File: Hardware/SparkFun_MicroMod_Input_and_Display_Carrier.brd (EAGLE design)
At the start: 57.1 x 82.5 mm, 72 parts, among them J1 MICROMOD-2222-C, J2 MICRO-SD, J3 USB-C_Prog, J4 AVR_SPI_PROG_3X2TESTPOINTS, J5 2.4" TFT, J6 QWIIC_RIGHT_ANGLE, Q1 1.1A/60V/600mΩ, U2 ATTINY84, U5 AP7361C-33FGE

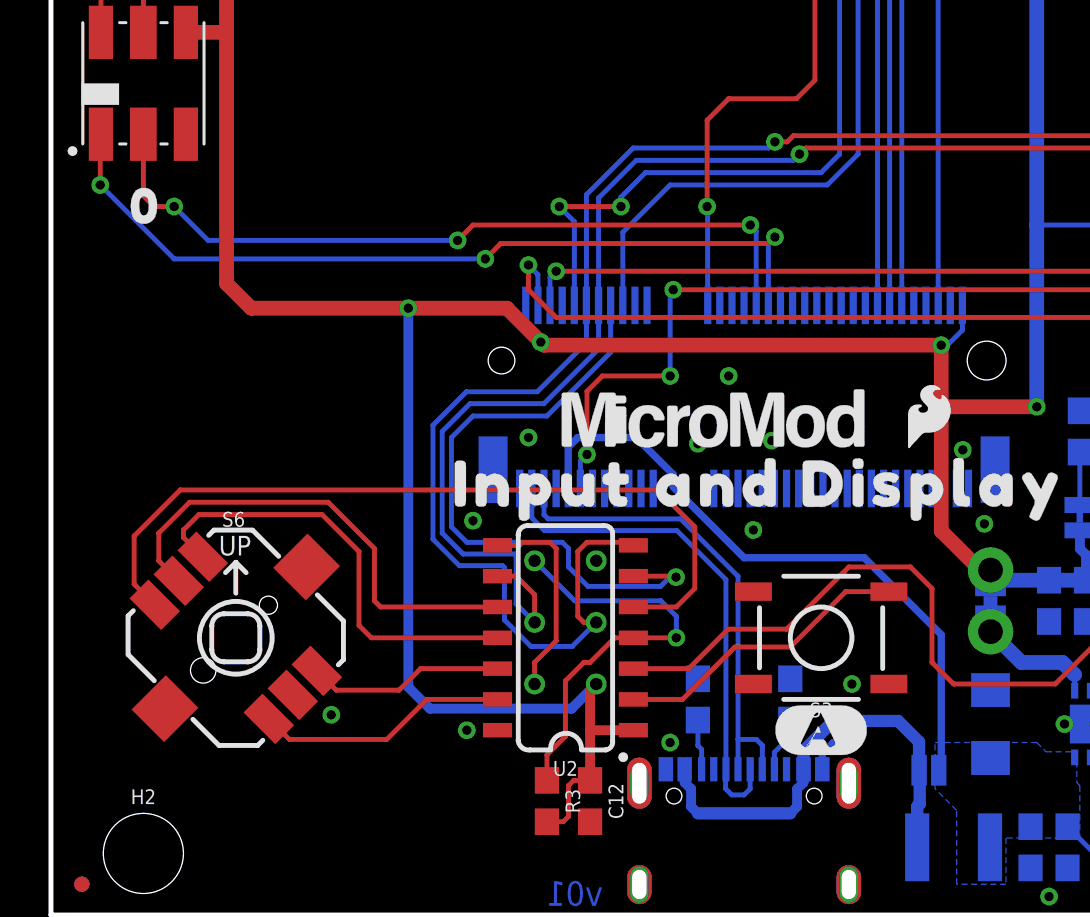
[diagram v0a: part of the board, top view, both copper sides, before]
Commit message: Pre-review changes
Added SWD connector
Updated SPI names
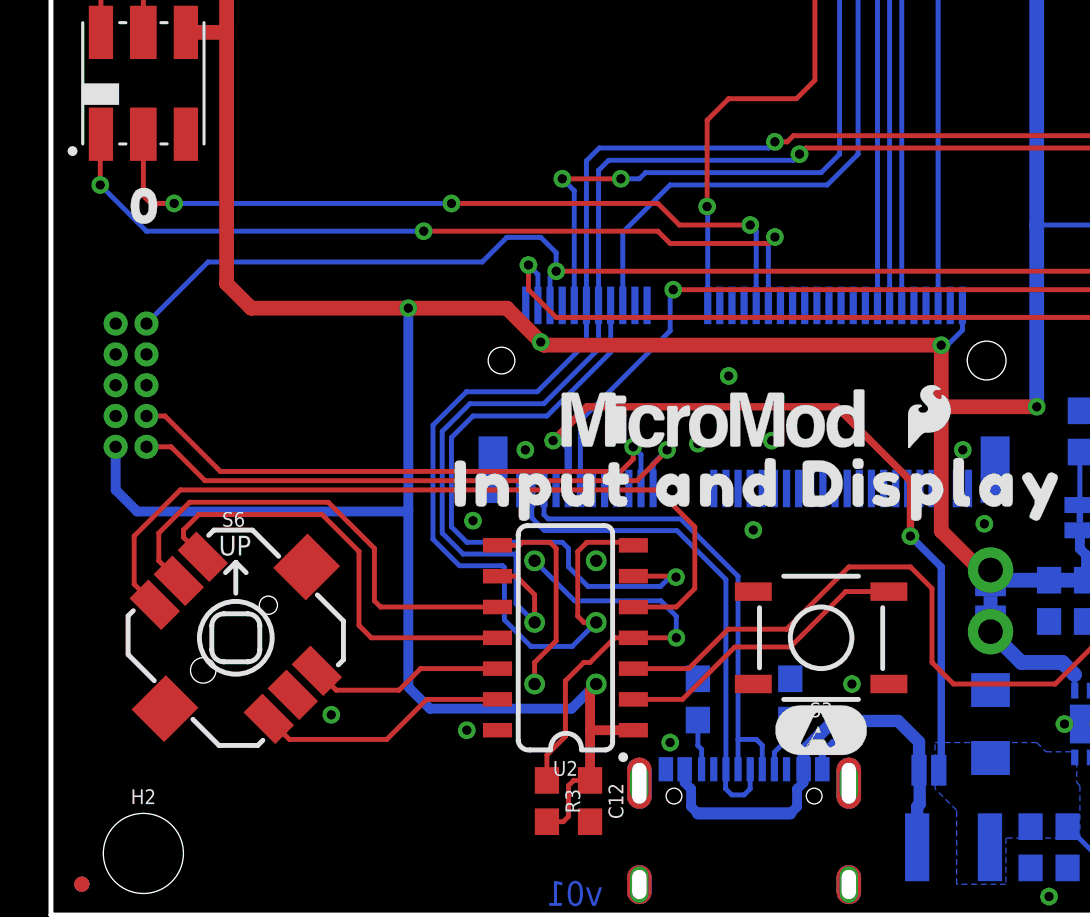
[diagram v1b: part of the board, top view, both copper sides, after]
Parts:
- added J7: CORTEX_JTAG_DEBUG, SparkFun-Connectors:2X5-PTH-1.27MM-NO_SILK
- added U$14: (no value), output:#BYP#0
- added U$15: (no value), output:#SWD#0
- H5: value STAND-OFF-REFLOW2.5MM_TALL -> STAND-OFF
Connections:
- net SPI_MISO renamed SPI_CIPO
- net SPI_MOSI renamed SPI_COPI
- removed net N$17: J1.23
- removed net N$18: J1.21
- new net SWDCK: J1.21, J7.4
- new net SWDIO: J1.23, J7.2
- net !RESET: now also J7.10
- net 3.3V: now also J7.1
- net GND: now also J7.3, J7.5, J7.9
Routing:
- net SWDIO: track 0.00 -> 24.4 mm, vias 0 -> 1
- net SWDCK: track 0.00 -> 23.6 mm, vias 0 -> 1
- net !RESET: track 38.1 -> 57.5 mm
- net 3.3V: track 251.4 -> 265.6 mm
- net VIN: track 29.0 -> 34.0 mm, vias 0 -> 2
- net !BOOT: track 50.5 -> 48.9 mm, vias 4 -> 2
- net SDA: track 71.0 -> 71.8 mm
- net SCL: track 62.2 -> 62.8 mm
- net LED_DATA: track 34.5 -> 34.0 mm
- net LED_CLK: track 32.0 -> 31.5 mm

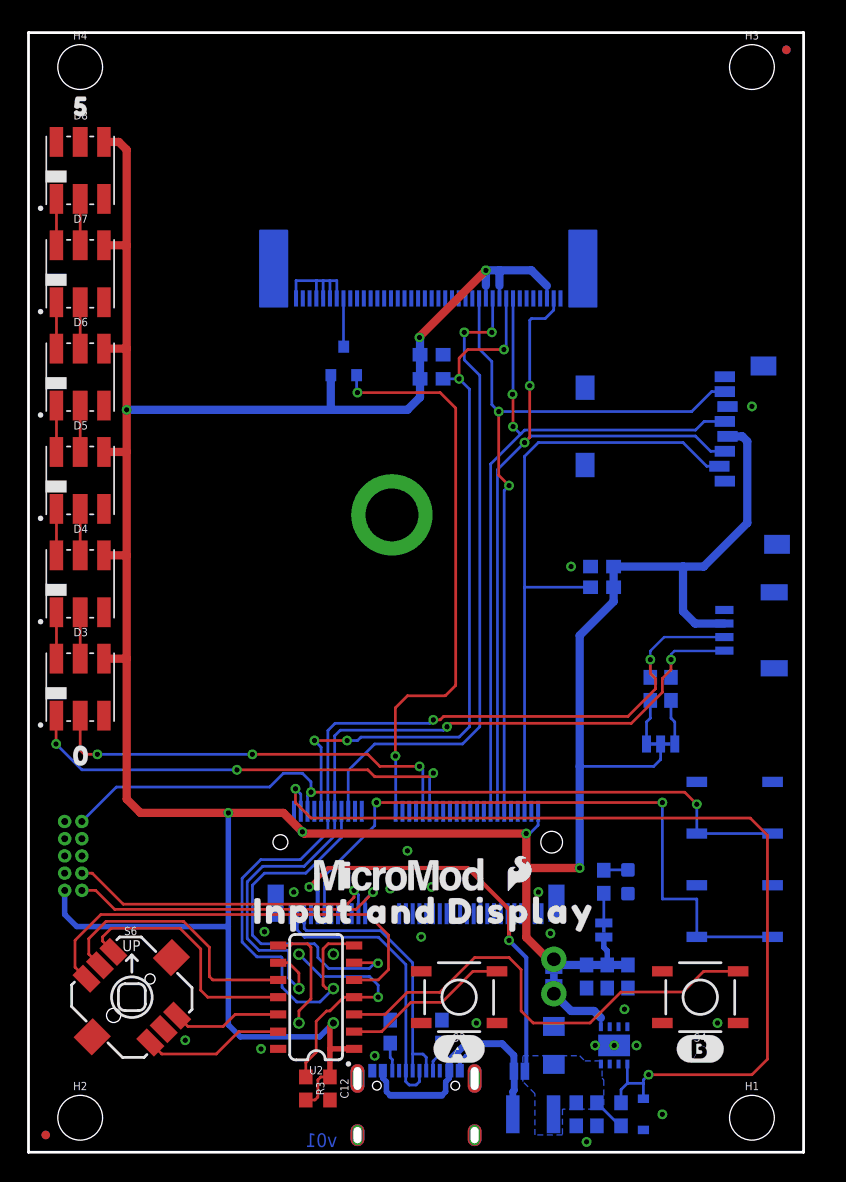
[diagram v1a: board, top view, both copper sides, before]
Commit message: Post review changes
- Added notes for jumpers
- Changed SPI_CS to SD_CS label
- Connected display reset to IO
- Added NO jumper between MicroMod and regulator enable
- Added Buzzer to PWM1
- Broke out A0/1, RX1/TX1, CAN-RX/TX, 3.3V, and GND
- Added name on back of the board
- Fixed or corrected DRC errors
- Fixed non-mitered corners
- Moved reset and boot buttons
- Added indicator for "UP" on 5-way switch
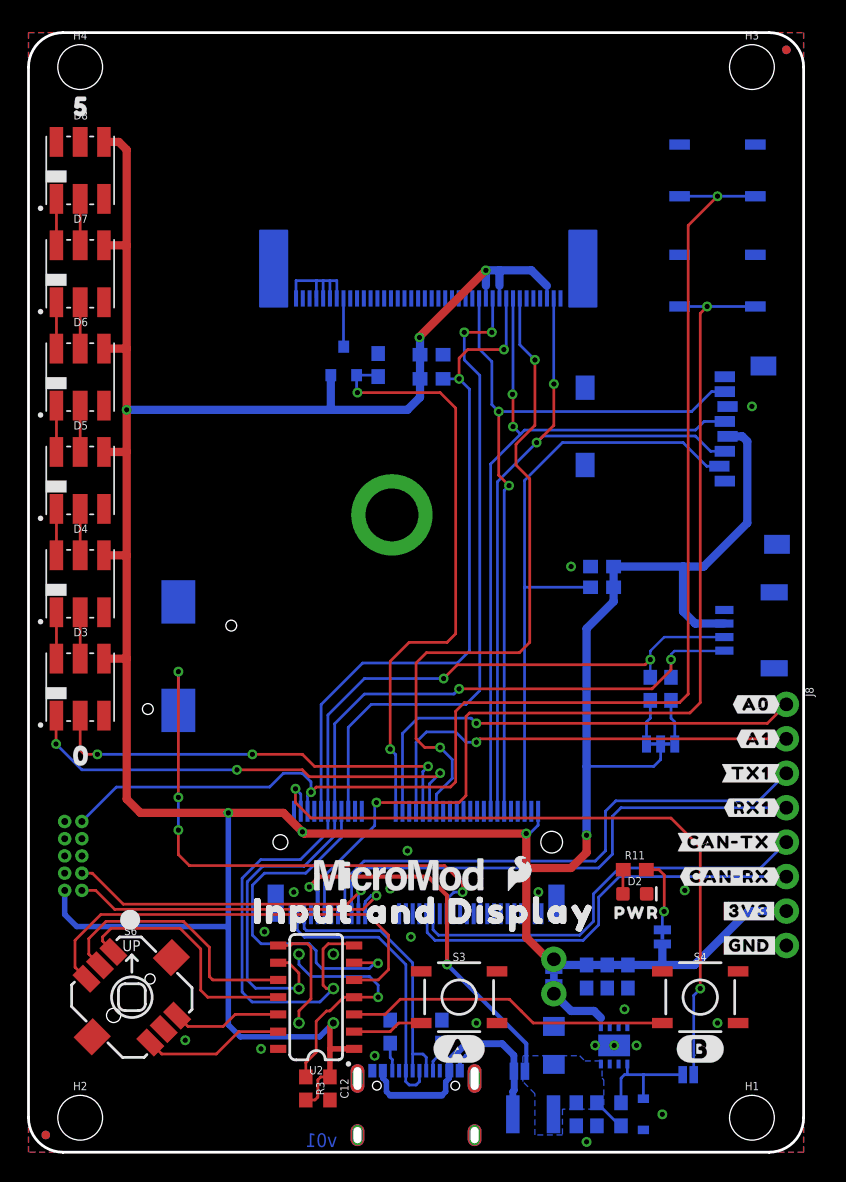
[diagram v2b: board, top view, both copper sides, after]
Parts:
- added 3V3_EN: (no value), SparkFun-Jumpers:SMT-JUMPER_2_NO_SILK
- added J8: (no value), SparkFun-Connectors:1X08_NO_SILK
- added LS1: Buzzer, SparkFun-Electromechanical:BUZZER-CCV
- added R9: 10k, SparkFun-Resistors:0603
- added U$16, U$17: (no value), output:INPUT_AND_DISPLAY0
- added U$19: (no value), output:#PWR#0
- added U$20: (no value), output:#3V3_CTRL#0
- added U$21: (no value), output:#PWM1#0
- added U$22, U$23: (no value), output:#A0#0
- added U$24, U$25: (no value), output:#A1#0
- added U$26, U$27: (no value), output:#TX1#0
- added U$28, U$31: (no value), output:#3V3#0
- added U$29, U$30: (no value), output:#GND#0
- added U$32, U$33: (no value), output:#RX1#0
- added U$34, U$35: (no value), output:#CAN#RX#0
- added U$36, U$37: (no value), output:#CAN#TX#0
- J6: value QWIIC_RIGHT_ANGLE -> QWIIC_RA
- moved S1 47.0 mm to (50.8, 72.4)
- moved U$4 46.6 mm to (50.8, 60.6)
- moved S2 46.5 mm to (50.8, 64.3)
- moved U$9 39.4 mm to (50.8, 69.0)
- moved PWR 4.35 mm to (46.7, 15.9)
- moved R11 2.45 mm to (44.7, 20.8), flipped to the top, turned to 0 degrees
- moved LOGO1 1.53 mm to (11.4, 54.4)
- moved U$13 1.31 mm to (44.8, 17.7), flipped to the top, turned to 0 degrees
- moved D2 1.02 mm to (44.7, 19.1), flipped to the top, turned to 0 degrees
- turned S3 to 0 degrees
- turned S4 to 0 degrees
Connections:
- net SPI_!CS renamed SD_!CS
- removed net DISP_TE: J1.47
- new net A0: J1.34, J8.1
- new net A1: J1.38, J8.2
- new net BUZZER: J1.47, LS1.-
- new net CAN-RX: J1.41, J8.6
- new net CAN-TX: J1.43, J8.5
- new net ENABLE: 3V3_EN.2, D1.C, R5.1, U5.5
- new net RX1: J1.19, J8.4
- new net TX1: J1.17, J8.3
- net 3.3V: now also J8.7
- net 3.3V_EN: now also 3V3_EN.1; no longer D1.C, R5.1, U5.5
- net DISP_!RST: now also J1.44
- net DISP_BL: now also R9.2
- net GND: now also J8.8, LS1.+, R9.1
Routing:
- net DISP_!RST: track 0.00 -> 49.0 mm, vias 0 -> 2
- net BUZZER: track 0.00 -> 41.3 mm, vias 0 -> 4
- net !RESET: track 57.5 -> 97.9 mm
- net TX1: track 0.00 -> 40.0 mm
- net RX1: track 0.00 -> 38.4 mm
- net A0: track 0.00 -> 35.3 mm, vias 0 -> 1
- net A1: track 0.00 -> 33.1 mm, vias 0 -> 1
- net CAN-TX: track 0.00 -> 31.4 mm
- net CAN-RX: track 0.00 -> 31.3 mm
- net !BOOT: track 48.9 -> 75.1 mm
- net 3.3V_EN: track 70.5 -> 51.0 mm
- net BTN_B: track 35.4 -> 23.9 mm
- net 3.3V: track 265.6 -> 277.1 mm
- net ENABLE: track 0.00 -> 9.02 mm
- net BTN_A: track 12.4 -> 5.21 mm
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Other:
- outline, holes or cut-outs redrawn

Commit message: QC Fixes
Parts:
- added TP1: (no value), SparkFun-Connectors:PAD.03X.03
- moved H5 4.68 mm to (24.6, 42.9)
- moved U$13 3.18 mm to (44.8, 20.8)
- moved R11 3.05 mm to (44.7, 17.8)
- moved D3 1.00 mm to (3.81, 33.3)
- moved D4 1.00 mm to (3.81, 40.9)
- moved D5 1.00 mm to (3.81, 48.5)
- moved D6 1.00 mm to (3.81, 56.1)
- moved D8 1.00 mm to (3.81, 71.4)
- moved U$17 1.00 mm to (2.54, 53.6)
- moved U$7 1.00 mm to (3.94, 28.2)
- moved U$8 1.00 mm to (3.94, 76.1)
- moved D7 1.00 mm to (3.81, 63.8)
- moved U$21 0.38 mm to (16.8, 36.6)
- moved D2 0.25 mm to (44.7, 19.3)
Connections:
- net SWDCK: now also TP1.P$1
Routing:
- net SWDCK: track 23.7 -> 27.5 mm
- net N$21: track 5.58 -> 2.76 mm
- net LED_CLK: track 32.2 -> 31.1 mm
- net 3.3V: track 277.1 -> 276.1 mm

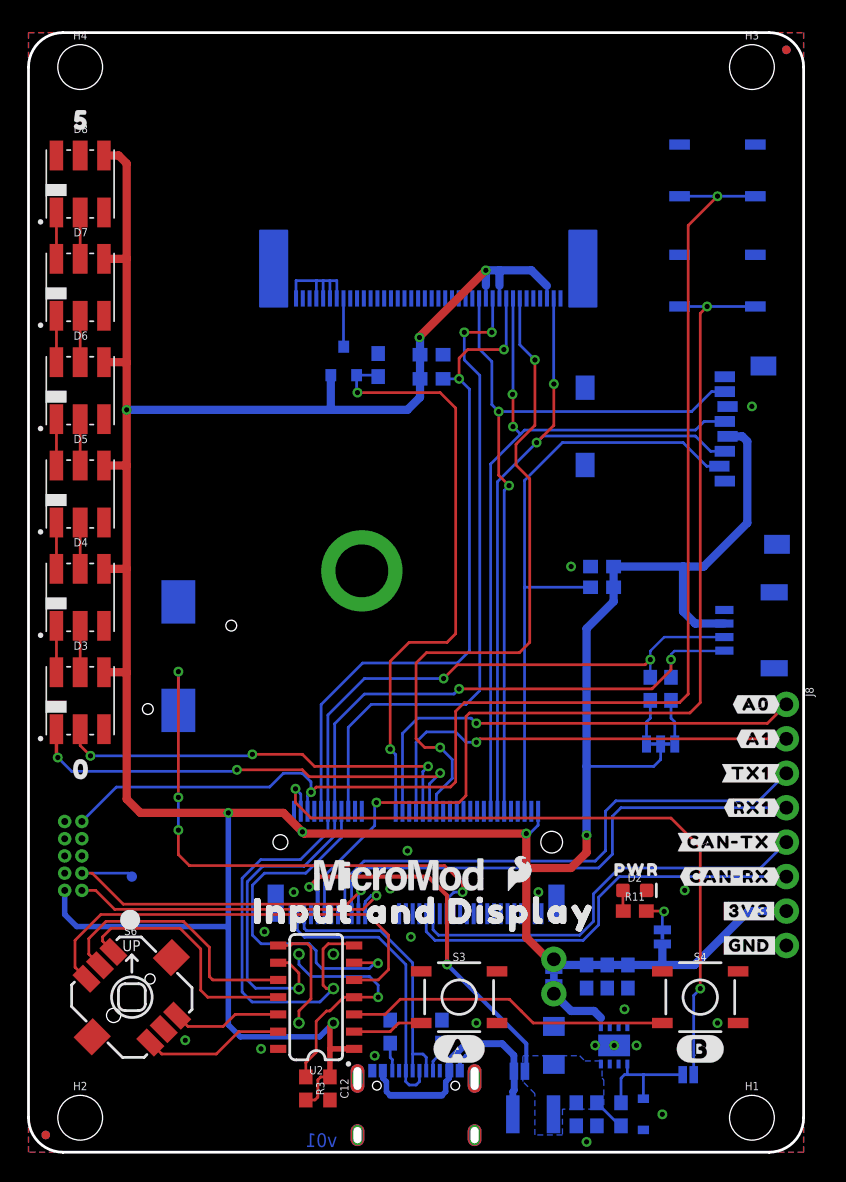
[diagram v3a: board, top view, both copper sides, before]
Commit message: v01 update
-Added 10ohm resistor to backlight
-Added 10k pullup to tft reset
-Connected Attiny reset to MM reset
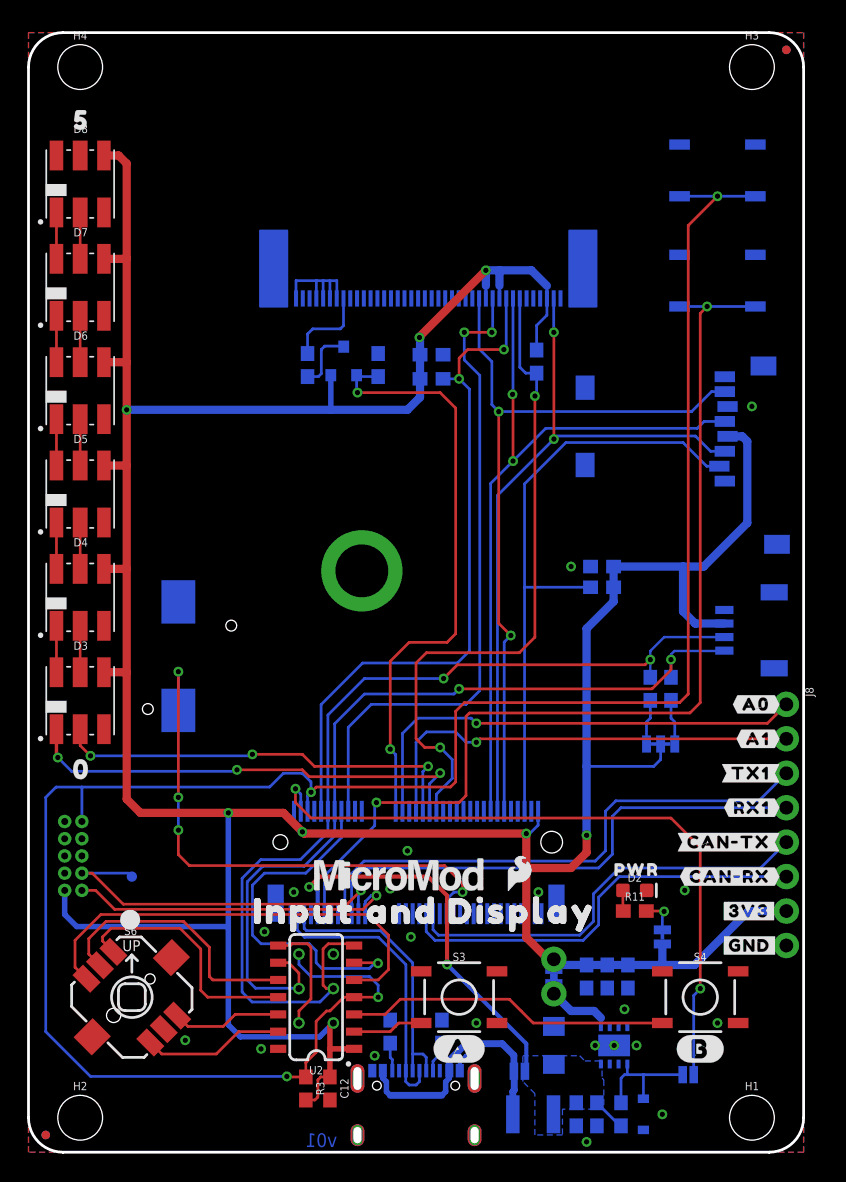
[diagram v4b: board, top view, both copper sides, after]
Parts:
- added R10: 10k, SparkFun-Resistors:0603
- added R12: 10, SparkFun-Resistors:0603
- Q1: value 1.1A/60V/600mΩ -> 1.1A/600mΩ
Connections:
- removed net !RST_ATTINY: J4.5, R3.1, U2.4
- removed net N$8: J5.8, Q1.3
- new net N$3: J5.8, R12.1
- new net N$4: Q1.3, R12.2
- net !RESET: now also J4.5, R3.1, U2.4
- net 3.3V: now also R10.2
- net DISP_!RST: now also R10.1
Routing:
- net !RESET: track 97.9 -> 158.1 mm, vias 2 -> 4
- net !RST_ATTINY: track 17.9 -> 0.00 mm, vias 1 -> 0
- net N$3: track 0.00 -> 6.35 mm
- net N$4: track 0.00 -> 4.66 mm
- net 3.3V: track 276.1 -> 280.2 mm
- net N$8: track 3.56 -> 0.00 mm
- net SPI_COPI: track 54.1 -> 52.7 mm
- net SPI_SCK: track 54.5 -> 55.4 mm

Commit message: v10
Moved display cable back slightly
Moved A and B buttons closer together
Moved measures jumper away from button A
Added silk to display outline
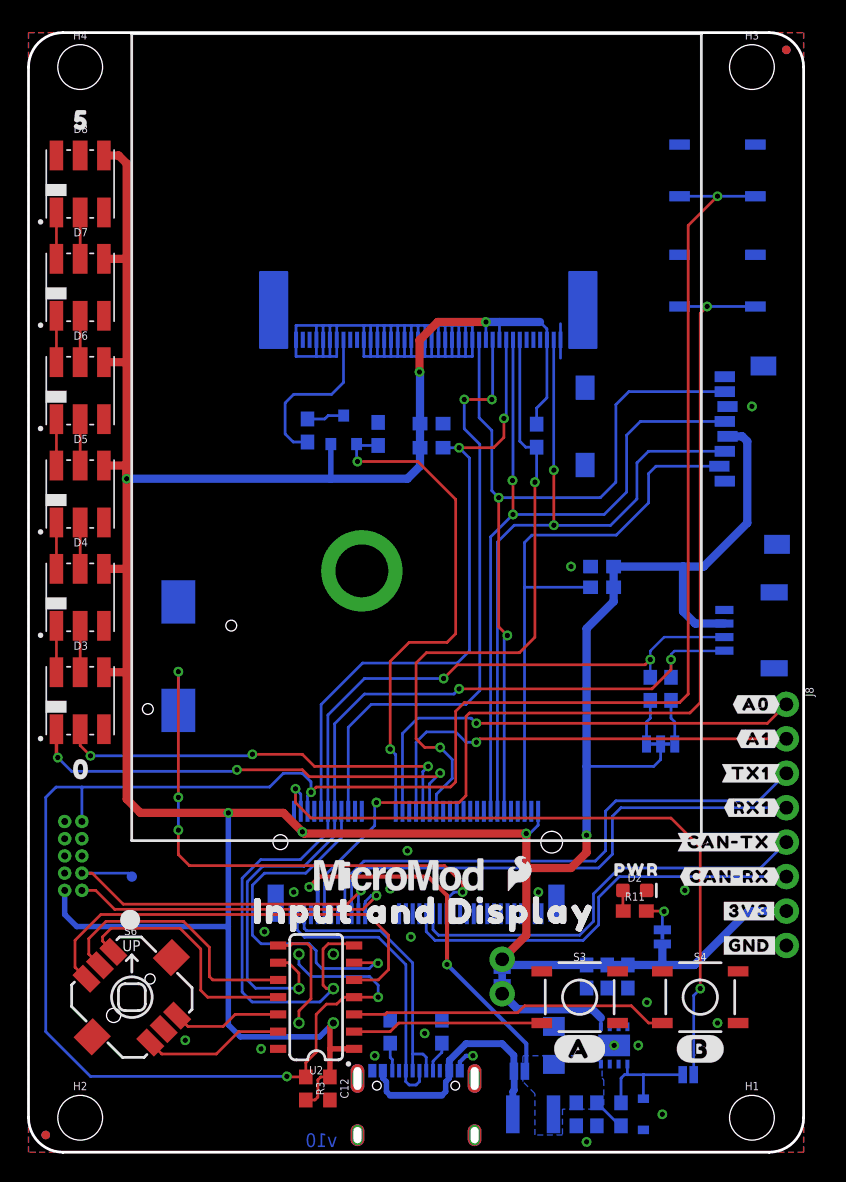
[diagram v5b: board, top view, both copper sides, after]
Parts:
- moved S3 8.89 mm to (40.6, 11.4)
- moved U$5 8.89 mm to (40.6, 7.62)
- moved R10 5.46 mm to (37.5, 52.8)
- moved C7 5.08 mm to (29.7, 53.7)
- moved R4 5.08 mm to (29.7, 51.9)
- moved Q1 5.08 mm to (23.2, 53.2)
- moved R9 5.08 mm to (25.8, 53.0)
- moved R12 4.83 mm to (20.6, 53.2), turned to 90 degrees
- moved MEAS 3.81 mm to (34.9, 13.0)
- moved U$11 3.81 mm to (33.3, 12.8)
- moved J5 3.05 mm to (29.5, 60.5)
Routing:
- net GND: track 11.4 -> 78.6 mm
- net BTN_A: track 5.21 -> 14.1 mm
- net 3.3V: track 280.2 -> 288.5 mm
- net DISP_BL: track 44.3 -> 38.1 mm
- net N$3: track 6.35 -> 12.3 mm
- net N$23: track 5.63 -> 9.44 mm
- net DISP_!CS: track 50.9 -> 47.8 mm
- net DISP_D/!C: track 48.5 -> 45.4 mm
- net DISP_!RST: track 48.8 -> 45.7 mm
- net SPI_CIPO: track 56.3 -> 59.0 mm
- net SD_!CS: track 45.4 -> 42.6 mm
- net SPI_COPI: track 52.7 -> 54.6 mm
- net N$4: track 4.66 -> 2.77 mm
- net SPI_SCK: track 55.4 -> 56.4 mm
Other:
- board text added: "v10"
- board text removed: "v01"
